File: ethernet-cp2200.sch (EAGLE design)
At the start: 21 parts, among them IC1 CP2200-GQ, Q1 20MHz

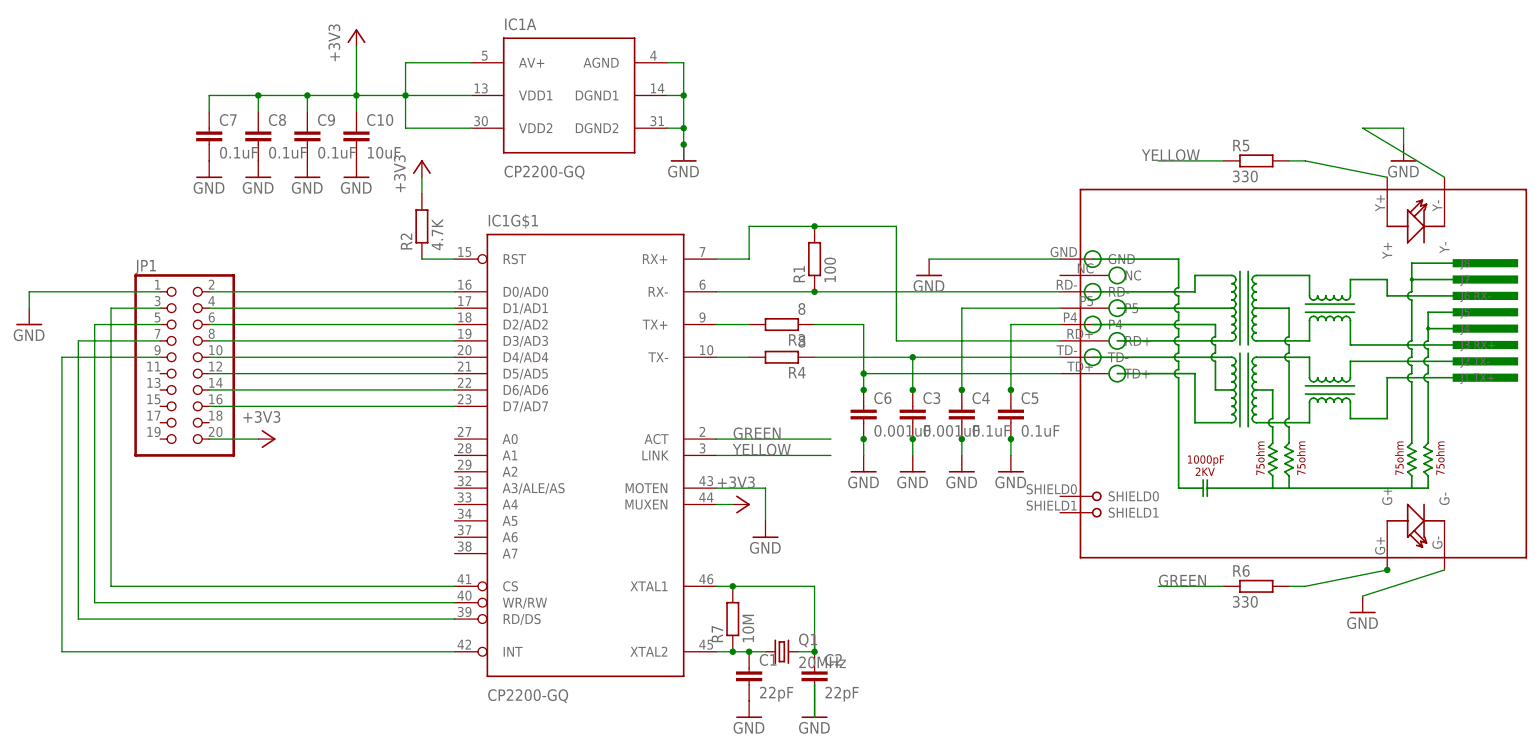
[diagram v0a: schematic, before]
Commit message: Connected the cp2200 board
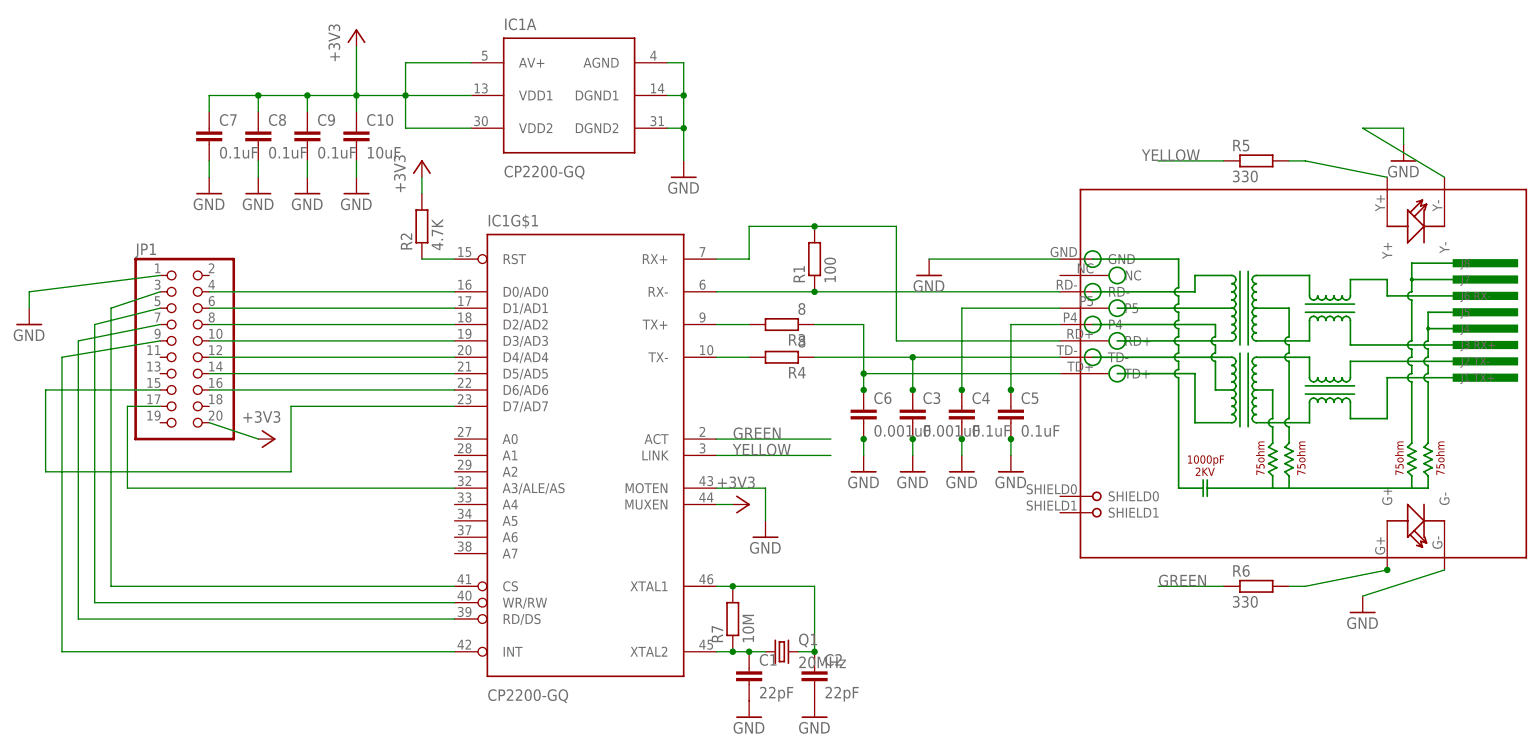
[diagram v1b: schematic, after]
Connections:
- removed net N$17: IC1A.AGND, IC1A.DGND1, IC1A.DGND2
- removed net N$24: IC1G$1.D7/AD7, JP1.16
- new net N$11: IC1G$1.A3/ALE/AS, JP1.17
- new net N$13: IC1G$1.D0/AD0, JP1.4
- net GND: now also IC1A.AGND, IC1A.DGND1, IC1A.DGND2
- net N$16: now also IC1G$1.D1/AD1, JP1.6; no longer IC1G$1.D0/AD0, JP1.2
- net N$18: now also IC1G$1.D2/AD2, JP1.8; no longer IC1G$1.D1/AD1, JP1.4
- net N$19: now also IC1G$1.D3/AD3, JP1.10; no longer IC1G$1.D2/AD2, JP1.6
- net N$20: now also IC1G$1.D4/AD4, JP1.12; no longer IC1G$1.D3/AD3, JP1.8
- net N$21: now also IC1G$1.D5/AD5, JP1.14; no longer IC1G$1.D4/AD4, JP1.10
- net N$22: now also IC1G$1.D6/AD6, JP1.16; no longer IC1G$1.D5/AD5, JP1.12
- net N$23: now also IC1G$1.D7/AD7, JP1.15; no longer IC1G$1.D6/AD6, JP1.14
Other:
- moved on the sheet: JP1
